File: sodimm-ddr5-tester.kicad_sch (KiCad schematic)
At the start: 24 parts, among them M1 Mech_Lightpipe_Mentor_1296.20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, U16 PCA9517A_TSSOP, U23 TS5A3359_VSSOP, U24 TS5A3359_VSSOP

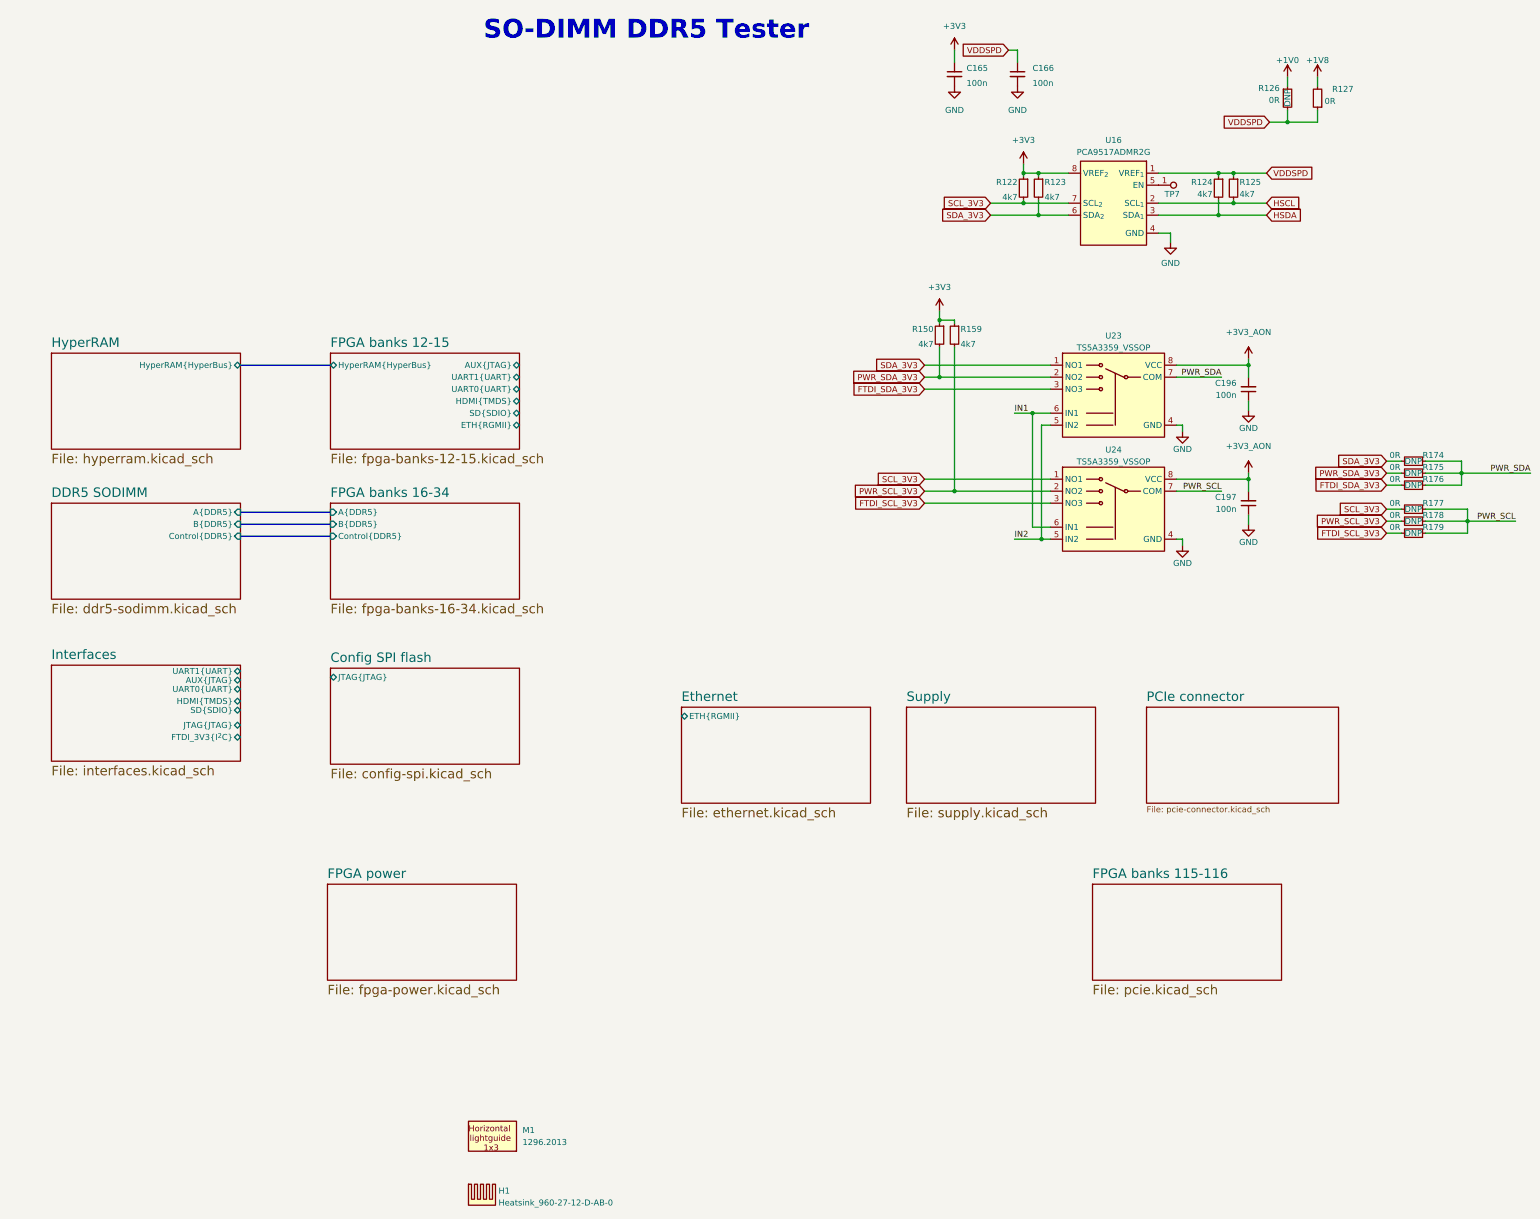
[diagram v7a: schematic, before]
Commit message: Finish creating hierarchical buses and structure, start reconnecting signals
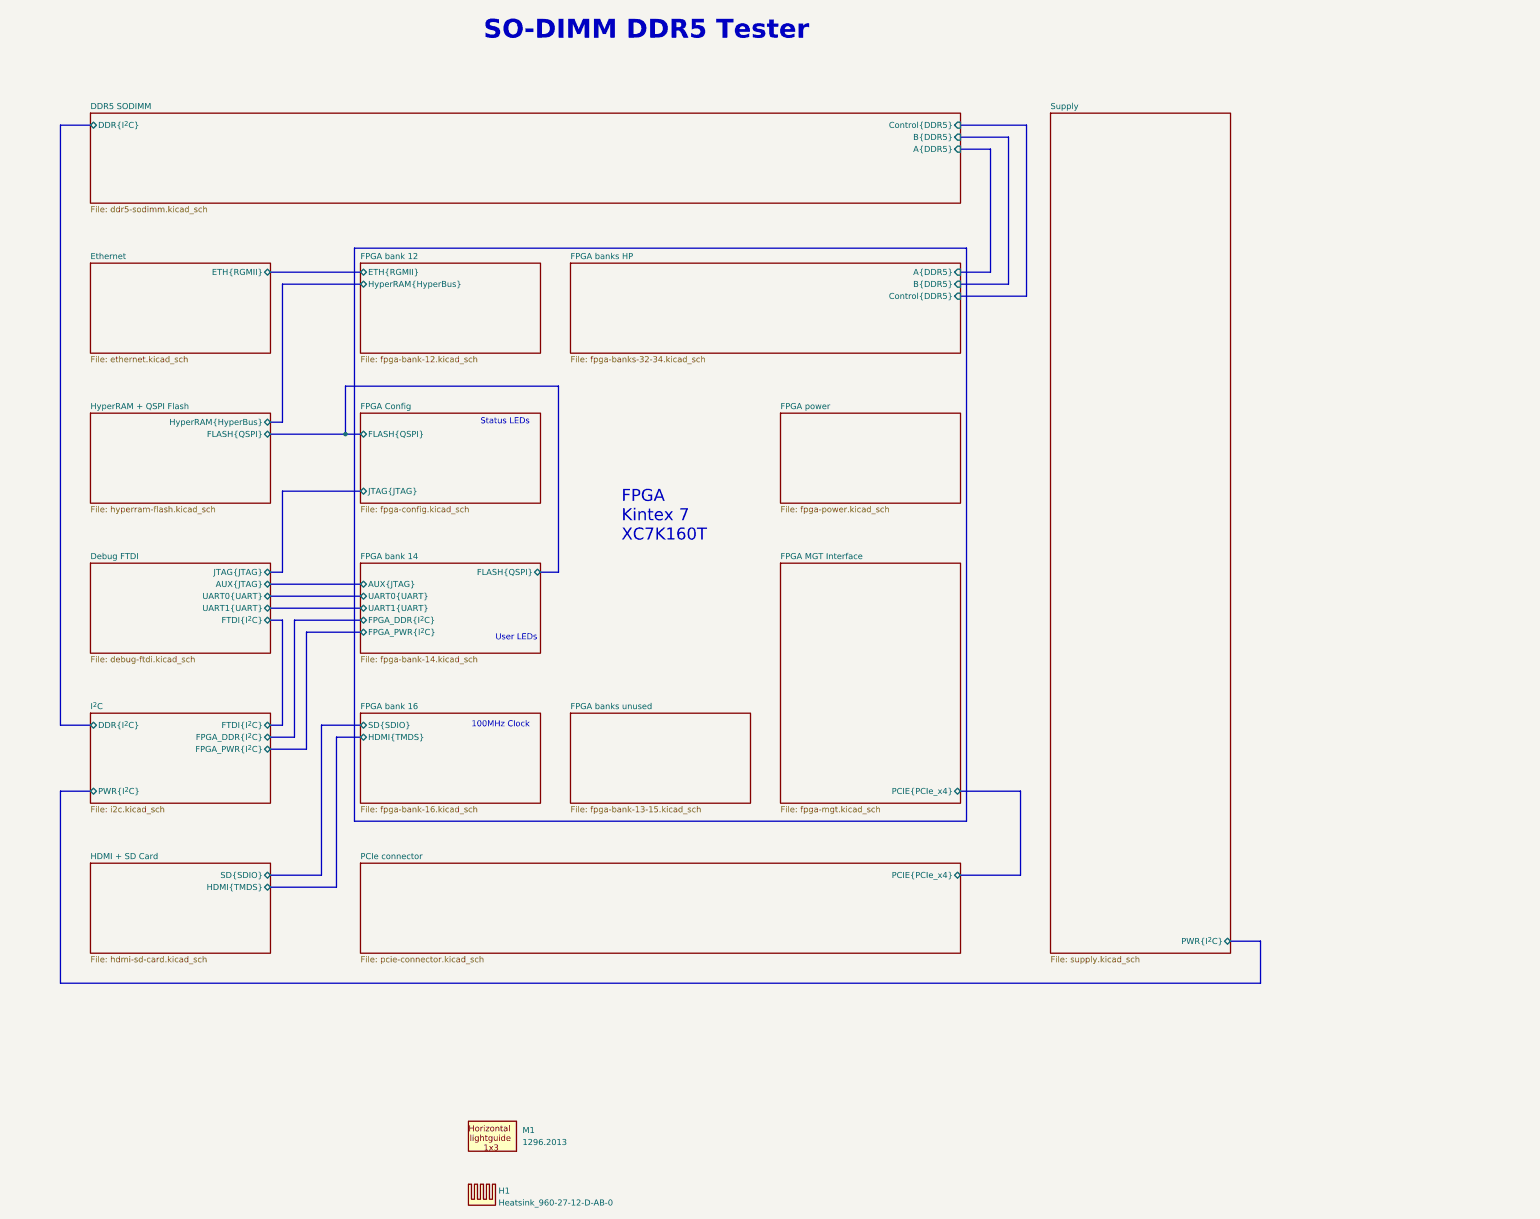
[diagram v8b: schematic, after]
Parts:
- removed C165, C166, C196, C197: C_100n_0402, sodimm-ddr5-tester-footprints:C_0402_1005Metric, symbol sodimm-ddr5-tester:C_100n_0402
- removed R122, R123, R124, R125, R150, R159: R_4k7_0402, sodimm-ddr5-tester-footprints:R_0402_1005Metric, symbol sodimm-ddr5-tester:R_4k7_0402
- removed R126, R127, R174, R175, R176, R177, R178, R179: R_0R_0402, sodimm-ddr5-tester-footprints:R_0402_1005Metric, symbol sodimm-ddr5-tester:R_0R_0402
- removed TP7: TP_1mm_SMD, sodimm-ddr5-tester-footprints:TP_SMD_1mm, symbol sodimm-ddr5-tester:TP_1mm_SMD
- removed U16: PCA9517A_TSSOP, sodimm-ddr5-tester-footprints:TSSOP-8_3x3mm_P0.65mm, symbol sodimm-ddr5-tester:PCA9517A_TSSOP
- removed U23, U24: TS5A3359_VSSOP, sodimm-ddr5-tester-footprints:VSSOP-8_2.3x2mm_P0.5mm, symbol sodimm-ddr5-tester:TS5A3359_VSSOP
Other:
- sheet Config SPI flash renamed FPGA Config
- sheet FPGA banks 115-116 renamed FPGA MGT Interface
- sheet FPGA banks 16-34 renamed FPGA banks HP
- sheet HyperRAM renamed HyperRAM + QSPI Flash
- sheet Interfaces renamed Debug FTDI
- removed sheet FPGA banks 12-15
- added sheet FPGA bank 12 (fpga-bank-12.kicad_sch)
- added sheet FPGA bank 14 (fpga-bank-14.kicad_sch)
- added sheet FPGA bank 16 (fpga-bank-16.kicad_sch)
- added sheet FPGA banks unused (fpga-bank-13-15.kicad_sch)
- added sheet HDMI + SD Card (hdmi-sd-card.kicad_sch)
- added sheet I^{2}C (i2c.kicad_sch)
- sheet DDR5 SODIMM ports: added DDR{I^{2}C}; removed none
- sheet Debug FTDI: file interfaces.kicad_sch -> debug-ftdi.kicad_sch
- sheet Debug FTDI ports: added FTDI{I^{2}C}; removed FTDI_3V3{I^{2}C}, HDMI{TMDS}, SD{SDIO}
- sheet FPGA Config: file config-spi.kicad_sch -> fpga-config.kicad_sch
- sheet FPGA Config ports: added FLASH{QSPI}; removed none
- sheet FPGA MGT Interface: file pcie.kicad_sch -> fpga-mgt.kicad_sch
- sheet FPGA MGT Interface ports: added PCIE{PCIe_x4}; removed none
- sheet FPGA banks HP: file fpga-banks-16-34.kicad_sch -> fpga-banks-32-34.kicad_sch
- sheet HyperRAM + QSPI Flash: file hyperram.kicad_sch -> hyperram-flash.kicad_sch
- sheet HyperRAM + QSPI Flash ports: added FLASH{QSPI}; removed none
- sheet PCIe connector ports: added PCIE{PCIe_x4}; removed none
- sheet Supply ports: added PWR{I^{2}C}; removed none
- note added: "100MHz Clock"
- note added: "FPGA Kintex 7 XC7K160T"
- note added: "Status LEDs"
- note added: "User LEDs"
